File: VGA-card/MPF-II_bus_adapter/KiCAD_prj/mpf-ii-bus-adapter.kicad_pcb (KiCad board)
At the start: 2 copper layers, 98.5 x 35.6 mm, 36 parts, among them J1 Bus_Apple_II_Card_Side, J10 USER1_Sel, J11 INH_Sel, J12 RDY_Sel, J13 COLREF_Sel, J14 IOSTRB_Sel, J15 Q3_Sel, J16 Pin, J17 Pin, J18 Pin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

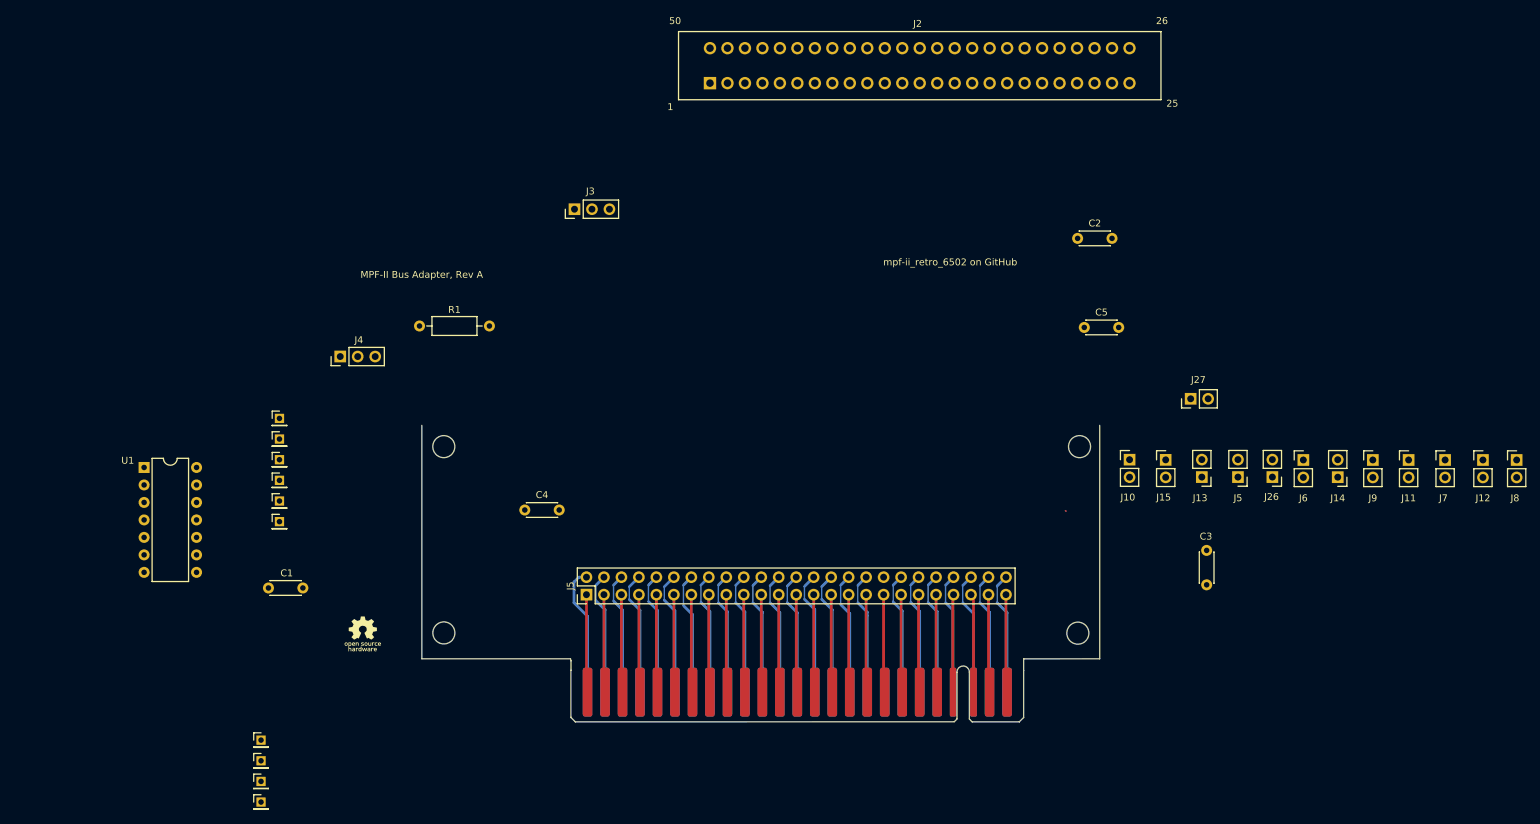
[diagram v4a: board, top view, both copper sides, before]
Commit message: Bus pin-header connector PCB
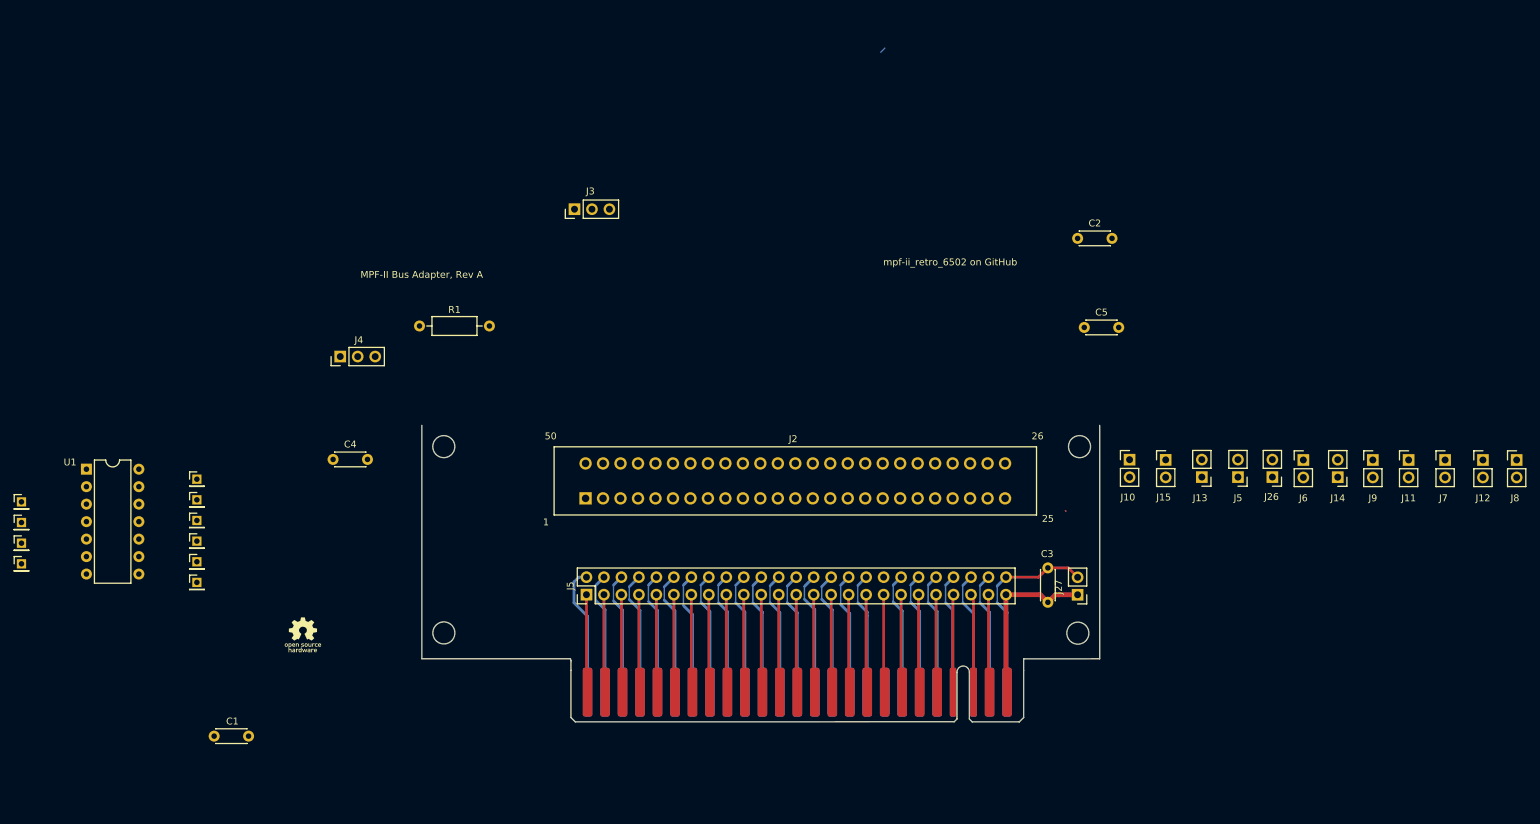
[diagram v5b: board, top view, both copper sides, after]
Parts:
- moved J2 63.0 mm to (118.7, 87.8)
- moved J16 49.1 mm to (36.7, 88.3)
- moved J17 49.1 mm to (36.7, 94.3)
- moved J24 49.1 mm to (36.7, 97.3)
- moved J25 49.1 mm to (36.7, 91.3)
- moved J27 32.9 mm to (190.2, 101.8), turned to 180 degrees
- moved C4 28.8 mm to (82.0, 82.2)
- moved C3 23.2 mm to (185.9, 102.9)
- moved C1 22.9 mm to (69.7, 122.4)
- moved J18 14.9 mm to (62.2, 97.0)
- moved J19 14.9 mm to (62.2, 91.0)
- moved J20 14.9 mm to (62.2, 85.0)
- moved J21 14.9 mm to (62.2, 88.0)
- moved J22 14.9 mm to (62.2, 94.0)
- moved J23 14.9 mm to (62.2, 100.0)
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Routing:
- net GND: track 18.1 -> 29.6 mm
- net +5V: track 14.2 -> 25.6 mm
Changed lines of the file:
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@@
 	(footprint "Capacitor_THT:C_Disc_D4.3mm_W1.9mm_P5.00mm"
 		(layer "F.Cu")
-		(at 208.94 100.4 90)
+		(at 185.87 102.94 90)
 		(descr "C, Disc series, Radial, pin pitch=5.00mm, , diameter*width=4.3*1.9mm^2, Capacitor, http://www.vishay.com/docs/45233/krseries.pdf")
 		(tags "C Disc series Radial pin pitch 5.00mm  diameter 4.3mm width 1.9mm Capacitor")
@@
 	(footprint "Capacitor_THT:C_Disc_D4.3mm_W1.9mm_P5.00mm"
 		(layer "F.Cu")
-		(at 109.86 89.53)
+		(at 82 82.18)
 		(descr "C, Disc series, Radial, pin pitch=5.00mm, , diameter*width=4.3*1.9mm^2, Capacitor, http://www.vishay.com/docs/45233/krseries.pdf")
 		(tags "C Disc series Radial pin pitch 5.00mm  diameter 4.3mm width 1.9mm Capacitor")
@@
 	(footprint "LOGO"
 		(layer "F.Cu")
-		(at 86.308751 107.644678)
+		(at 77.608751 107.784678)
 		(property "Reference" "G***"
 			(at 0 0 0)
@@
 	(footprint "Connector_PinHeader_2.00mm:PinHeader_1x01_P2.00mm_Vertical"
 		(layer "F.Cu")
-		(at 74.21 79.22)
+		(at 62.21 88.05)
 		(descr "Through hole straight pin header, 1x01, 2.00mm pitch, single row")
 		(tags "Through hole pin header THT 1x01 2.00mm single row")
@@
 	(footprint "Connector_PinHeader_2.00mm:PinHeader_1x01_P2.00mm_Vertical"
 		(layer "F.Cu")
-		(at 71.53 131.97)
+		(at 36.72 97.35)
 		(descr "Through hole straight pin header, 1x01, 2.00mm pitch, single row")
 		(tags "Through hole pin header THT 1x01 2.00mm single row")
@@
 	(footprint "Connector_PinHeader_2.00mm:PinHeader_1x01_P2.00mm_Vertical"
 		(layer "F.Cu")
-		(at 71.53 125.97)
+		(at 36.72 91.35)
 		(descr "Through hole straight pin header, 1x01, 2.00mm pitch, single row")
 		(tags "Through hole pin header THT 1x01 2.00mm single row")
@@
 	(footprint "PCM_MA_Connector_AppleII:EDAC_395-050-520-201_CounterClockwise"
 		(layer "F.Cu")
-		(at 136.77 27.5)
+		(at 118.69 87.84)
 		(descr "EDAC 395-050-520-201 Card Edge Connector - counter-clockwise pin numbering")
 		(tags "395-050-520-201 apple ii")
@@
 	(footprint "Capacitor_THT:C_Disc_D4.3mm_W1.9mm_P5.00mm"
 		(layer "F.Cu")
-		(at 77.61 100.86 180)
+		(at 69.72 122.39 180)
 		(descr "C, Disc series, Radial, pin pitch=5.00mm, , diameter*width=4.3*1.9mm^2, Capacitor, http://www.vishay.com/docs/45233/krseries.pdf")
 		(tags "C Disc series Radial pin pitch 5.00mm  diameter 4.3mm width 1.9mm Capacitor")
@@
 	(footprint "Connector_PinHeader_2.00mm:PinHeader_1x01_P2.00mm_Vertical"
 		(layer "F.Cu")
-		(at 74.21 88.22)
+		(at 62.21 97.05)
 		(descr "Through hole straight pin header, 1x01, 2.00mm pitch, single row")
 		(tags "Through hole pin header THT 1x01 2.00mm single row")
@@
 	(footprint "Connector_PinHeader_2.00mm:PinHeader_1x01_P2.00mm_Vertical"
 		(layer "F.Cu")
-		(at 74.21 91.22)
+		(at 62.21 100.05)
 		(descr "Through hole straight pin header, 1x01, 2.00mm pitch, single row")
 		(tags "Through hole pin header THT 1x01 2.00mm single row")
@@
 	(footprint "Connector_PinHeader_2.54mm:PinHeader_1x02_P2.54mm_Vertical"
 		(layer "F.Cu")
-		(at 206.62 73.37 90)
+		(at 190.19 101.845 180)
 		(descr "Through hole straight pin header, 1x02, 2.54mm pitch, single row")
 		(tags "Through hole pin header THT 1x02 2.54mm single row")
 		(property "Reference" "J27"
-			(at 2.76 1.115 0)
+			(at 2.76 1.115 90)
 			(layer "F.SilkS")
 			(effects
@@
 		)
 		(property "Value" "PWR"
-			(at 0 4.87 90)
+			(at 0 4.87 0)
 			(layer "F.Fab")
 			(hide yes)
@@
 		)
 		(property "Footprint" "Connector_PinHeader_2.54mm:PinHeader_1x02_P2.54mm_Vertical"
-			(at 0 0 90)
+			(at 0 0 180)
 			(unlocked yes)
 			(layer "F.Fab")
@@
 		)
 		(property "Datasheet" ""
-			(at 0 0 90)
+			(at 0 0 180)
 			(unlocked yes)
 			(layer "F.Fab")
@@
 		)
 		(property "Description" "Generic connector, single row, 01x02, script generated"
-			(at 0 0 90)
+			(at 0 0 180)
 			(unlocked yes)
 			(layer "F.Fab")
@@
 		(attr through_hole)
 		(fp_line
-			(start -1.33 -1.33)
-			(end 0 -1.33)
+			(start 1.33 1.27)
+			(end 1.33 3.87)
 			(stroke
 				(width 0.12)
@@
 		)
 		(fp_line
-			(start -1.33 0)
-			(end -1.33 -1.33)
+			(start -1.33 3.87)
+			(end 1.33 3.87)
 			(stroke
 				(width 0.12)
@@
 		)
 		(fp_line
-			(start 1.33 1.27)
-			(end 1.33 3.87)
+			(start -1.33 1.27)
+			(end 1.33 1.27)
 			(stroke
 				(width 0.12)
@@
 		(fp_line
 			(start -1.33 1.27)
-			(end 1.33 1.27)
+			(end -1.33 3.87)
 			(stroke
 				(width 0.12)
@@
 		)
 		(fp_line
-			(start -1.33 1.27)
-			(end -1.33 3.87)
+			(start -1.33 0)
+			(end -1.33 -1.33)
 			(stroke
 				(width 0.12)
@@
 		)
 		(fp_line
-			(start -1.33 3.87)
-			(end 1.33 3.87)
+			(start -1.33 -1.33)
+			(end 0 -1.33)
 			(stroke
 				(width 0.12)
@@
 		)
 		(fp_line
-			(start 1.8 -1.8)
-			(end -1.8 -1.8)
+			(start 1.8 4.35)
+			(end 1.8 -1.8)
 			(stroke
 				(width 0.05)
@@
 		)
 		(fp_line
-			(start -1.8 -1.8)
-			(end -1.8 4.35)
+			(start 1.8 -1.8)
+			(end -1.8 -1.8)
 			(stroke
 				(width 0.05)
@@
 		)
 		(fp_line
-			(start 1.8 4.35)
-			(end 1.8 -1.8)
+			(start -1.8 4.35)
+			(end 1.8 4.35)
 			(stroke
 				(width 0.05)
@@
 		)
 		(fp_line
-			(start -1.8 4.35)
-			(end 1.8 4.35)
+			(start -1.8 -1.8)
+			(end -1.8 4.35)
 			(stroke
 				(width 0.05)
@@
 		)
 		(fp_line
-			(start 1.27 -1.27)
-			(end 1.27 3.81)
+			(start 1.27 3.81)
+			(end -1.27 3.81)
 			(stroke
 				(width 0.1)
@@
 		)
 		(fp_line
-			(start -0.635 -1.27)
-			(end 1.27 -1.27)
+			(start 1.27 -1.27)
+			(end 1.27 3.81)
 			(stroke
 				(width 0.1)
@@
 		)
 		(fp_line
-			(start -1.27 -0.635)
-			(end -0.635 -1.27)
+			(start -0.635 -1.27)
+			(end 1.27 -1.27)
 			(stroke
 				(width 0.1)
@@
 		)
 		(fp_line
-			(start 1.27 3.81)
-			(end -1.27 3.81)
+			(start -1.27 3.81)
+			(end -1.27 -0.635)
 			(stroke
 				(width 0.1)
@@
 		)
 		(fp_line
-			(start -1.27 3.81)
-			(end -1.27 -0.635)
+			(start -1.27 -0.635)
+			(end -0.635 -1.27)
 			(stroke
 				(width 0.1)
@@
 		)
 		(fp_text user "${REFERENCE}"
-			(at 0 1.27 0)
+			(at 0 1.27 90)
 			(layer "F.Fab")
 			(effects
@@
 		)
 		(pad "1" thru_hole rect
-			(at 0 0 90)
+			(at 0 0 180)
 			(size 1.7 1.7)
 			(drill 1)
@@
 		)
 		(pad "2" thru_hole oval
-			(at 0 2.54 90)
+			(at 0 2.54 180)
 			(size 1.7 1.7)
 			(drill 1)
@@
 	(footprint "Connector_PinHeader_2.00mm:PinHeader_1x01_P2.00mm_Vertical"
 		(layer "F.Cu")
-		(at 71.53 122.97)
+		(at 36.72 88.35)
 		(descr "Through hole straight pin header, 1x01, 2.00mm pitch, single row")
 		(tags "Through hole pin header THT 1x01 2.00mm single row")
@@
 	(footprint "Connector_PinHeader_2.00mm:PinHeader_1x01_P2.00mm_Vertical"
 		(layer "F.Cu")
-		(at 71.53 128.97)
+		(at 36.72 94.35)
 		(descr "Through hole straight pin header, 1x01, 2.00mm pitch, single row")
 		(tags "Through hole pin header THT 1x01 2.00mm single row")
@@
 	(footprint "Connector_PinHeader_2.00mm:PinHeader_1x01_P2.00mm_Vertical"
 		(layer "F.Cu")
-		(at 74.21 76.22)
+		(at 62.21 85.05)
 		(descr "Through hole straight pin header, 1x01, 2.00mm pitch, single row")
 		(tags "Through hole pin header THT 1x01 2.00mm single row")
@@
 	(footprint "Package_DIP:DIP-14_W7.62mm"
 		(layer "F.Cu")
-		(at 54.54 83.35)
+		(at 46.16 83.6)
 		(descr "14-lead though-hole mounted DIP package, row spacing 7.62 mm (300 mils)")
 		(tags "THT DIP DIL PDIP 2.54mm 7.62mm 300mil")
@@
 	(footprint "Connector_PinHeader_2.00mm:PinHeader_1x01_P2.00mm_Vertical"
 		(layer "F.Cu")
-		(at 74.21 82.22)
+		(at 62.21 91.05)
 		(descr "Through hole straight pin header, 1x01, 2.00mm pitch, single row")
 		(tags "Through hole pin header THT 1x01 2.00mm single row")
@@
 	(footprint "Connector_PinHeader_2.00mm:PinHeader_1x01_P2.00mm_Vertical"
 		(layer "F.Cu")
-		(at 74.21 85.22)
+		(at 62.21 94.05)
 		(descr "Through hole straight pin header, 1x01, 2.00mm pitch, single row")
 		(tags "Through hole pin header THT 1x01 2.00mm single row")
@@
 	)
 	(segment
+		(start 186.96 101.85)
+		(end 187.55 101.85)
+		(width 0.7)
+		(layer "F.Cu")
+		(net 1)
+	)
+	(segment
 		(start 179.78 101.83)
 		(end 179.78 115.84)
-		(width 0.4)
+		(width 0.7)
 		(layer "F.Cu")
 		(net 1)
@@
 	)
 	(segment
+		(start 179.78 101.83)
+		(end 184.76 101.83)
+		(width 0.7)
+		(layer "F.Cu")
+		(net 1)
+	)
+	(segment
+		(start 187.555 101.845)
+		(end 190.19 101.845)
+		(width 0.7)
+		(layer "F.Cu")
+		(net 1)
+	)
+	(segment
+		(start 187.55 101.85)
+		(end 187.555 101.845)
+		(width 0.7)
+		(layer "F.Cu")
+		(net 1)
+	)
+	(segment
+		(start 190.155 101.83)
+		(end 190.19 101.795)
+		(width 0.4)
+		(layer "F.Cu")
+		(net 1)
+	)
+	(segment
+		(start 185.87 102.94)
+		(end 186.96 101.85)
+		(width 0.7)
+		(layer "F.Cu")
+		(net 1)
+	)
+	(segment
+		(start 184.76 101.83)
+		(end 185.87 102.94)
+		(width 0.7)
+		(layer "F.Cu")
+		(net 1)
+	)
+	(segment
+		(start 179.78 99.29)
+		(end 184.52 99.29)
+		(width 0.4)
+		(layer "F.Cu")
+		(net 2)
+	)
+	(segment
+		(start 184.52 99.29)
+		(end 185.87 97.94)
+		(width 0.4)
+		(layer "F.Cu")
+		(net 2)
+	)
+	(segment
+		(start 190.155 99.29)
+		(end 190.19 99.255)
+		(width 0.4)
+		(layer "F.Cu")
+		(net 2)
+	)
+	(segment
 		(start 188.42 89.63)
 		(end 188.5 89.71)
@@
 	)
 	(segment
+		(start 185.87 97.94)
+		(end 188.825 97.94)
+		(width 0.4)
+		(layer "F.Cu")
+		(net 2)
+	)
+	(segment
+		(start 188.825 97.94)
+		(end 190.19 99.305)
+		(width 0.4)
+		(layer "F.Cu")
+		(net 2)
+	)
+	(segment
 		(start 178.5 100.57)
 		(end 178.5 103)
@@
 	)
 	(segment
-		(start 73.88 81.89)
-		(end 74.21 82.22)
+		(start 61.88 90.72)
+		(end 62.21 91.05)
 		(width 0.2)
 		(layer "F.Cu")
@@
 	)
 	(segment
-		(start 73.62 76.81)
-		(end 74.21 76.22)
+		(start 61.62 85.64)
+		(end 62.21 85.05)
 		(width 0.2)
 		(layer "F.Cu")
@@
 	)
 	(segment
-		(start 74.08 79.35)
-		(end 74.21 79.22)
+		(start 62.08 88.18)
+		(end 62.21 88.05)
 		(width 0.2)
 		(layer "F.Cu")

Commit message: PCB
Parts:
- removed J18, J19, J20, J21, J22, J23, J24, J25: Pin, Connector_PinHeader_2.00mm:PinHeader_1x01_P2.00mm_Vertical
- J16: value Pin -> Conn_01x04_Pin; footprint Connector_PinHeader_2.00mm:PinHeader_1x01_P2.00mm_Vertical -> Connector_PinHeader_2.54mm:PinHeader_1x04_P2.54mm_Vertical
- J17: value Pin -> Conn_01x06_Pin; footprint Connector_PinHeader_2.00mm:PinHeader_1x01_P2.00mm_Vertical -> Connector_PinHeader_2.54mm:PinHeader_1x06_P2.54mm_Vertical
- moved G*** 106.5 mm to (184.1, 107.2)
- moved J17 75.1 mm to (111.8, 93.8)
- moved J16 60.3 mm to (97.0, 91.4)
- moved U1 54.0 mm to (100.1, 86.3)
- moved J10 48.1 mm to (150.1, 75.6), turned to 90 degrees
- moved J15 45.5 mm to (157.9, 75.7), turned to 90 degrees
- moved R1 43.4 mm to (136.0, 75.7), turned to 180 degrees
- moved C1 42.4 mm to (108.3, 104.9)
- moved J3 37.8 mm to (140.3, 75.7)
- moved J13 34.5 mm to (174.9, 75.8), turned to -90 degrees
- moved J4 34.5 mm to (116.5, 75.8)
- moved C2 33.6 mm to (168.8, 76.0), turned to 180 degrees
- moved C5 28.8 mm to (190.3, 91.8), turned to 90 degrees
- moved C4 22.9 mm to (104.5, 77.5), turned to -90 degrees
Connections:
- U1 pad 10: Net-(J22-Pin_1) -> Net-(J17-Pin_4)
- U1 pad 11: Net-(J19-Pin_1) -> Net-(J17-Pin_3)
- U1 pad 12: Net-(J21-Pin_1) -> Net-(J17-Pin_2)
- U1 pad 13: Net-(J20-Pin_1) -> Net-(J17-Pin_1)
- U1 pad 4: Net-(J25-Pin_1) -> Net-(J16-Pin_2)
- U1 pad 5: Net-(J17-Pin_1) -> Net-(J16-Pin_3)
- U1 pad 6: Net-(J24-Pin_1) -> Net-(J16-Pin_4)
- U1 pad 8: Net-(J23-Pin_1) -> Net-(J17-Pin_6)
- U1 pad 9: Net-(J18-Pin_1) -> Net-(J17-Pin_5)
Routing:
- net +5V: track 25.6 -> 179.9 mm
- net GND: track 29.6 -> 93.7 mm
- net Net-(J4-Pin_1): track 0.00 -> 24.3 mm
- net +12V: track 18.9 -> 37.1 mm
- net /IOSEL: track 15.0 -> 30.2 mm
- net Net-(J17-Pin_2): track 0.00 -> 8.02 mm
- net Net-(J17-Pin_6): track 0.00 -> 7.40 mm
- net Net-(J17-Pin_5): track 0.00 -> 7.33 mm
- net Net-(J17-Pin_3): track 0.00 -> 7.30 mm
- net Net-(J17-Pin_4): track 0.00 -> 7.16 mm
- net Net-(J17-Pin_1): track 0.00 -> 6.70 mm
- net Net-(J16-Pin_3): track 0.00 -> 3.13 mm
- net Net-(J16-Pin_1): track 0.00 -> 3.13 mm
- net Net-(J16-Pin_4): track 0.00 -> 3.13 mm
- net Net-(J16-Pin_2): track 0.00 -> 3.13 mm
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
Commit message: PCB updated
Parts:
- removed the J5 at (213.5, 84.7)
- moved J26 77.7 mm to (141.5, 95.5)
- moved J6 77.0 mm to (146.8, 93.0)
- moved J9 76.8 mm to (157.0, 93.0)
- moved J14 76.8 mm to (152.0, 95.5)
- moved J11 76.5 mm to (162.5, 93.0)
- moved J7 76.3 mm to (168.0, 93.0)
- moved J12 76.1 mm to (173.8, 93.0)
- moved J8 75.3 mm to (179.5, 93.0)
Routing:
- net /D1: track 17.7 -> 35.4 mm
- net /D0: track 17.7 -> 35.3 mm
- net /A1: track 14.2 -> 29.4 mm
- net /A0: track 17.6 -> 32.7 mm
- net +5V: track 179.9 -> 176.8 mm
- net Net-(J4-Pin_1): track 24.3 -> 26.9 mm
- net /EXTE: track 17.8 -> 17.0 mm

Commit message: PCB updated
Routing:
- net GND: track 94.0 -> 175.5 mm, vias 0 -> 1
- net /PHI1: track 17.9 -> 72.4 mm, vias 0 -> 1
- net /A_PHI0: track 0.00 -> 34.6 mm, vias 0 -> 1
- net /A8: track 14.2 -> 32.2 mm
- net /D3: track 17.7 -> 35.4 mm
- net /D4: track 17.9 -> 35.6 mm
- net /D6: track 17.7 -> 35.3 mm
- net /D5: track 17.7 -> 35.3 mm
- net /D2: track 17.9 -> 35.5 mm
- net /D7: track 17.7 -> 35.3 mm
- net /A2: track 14.2 -> 29.4 mm
- net /A5: track 14.2 -> 29.3 mm
- net /A7: track 14.2 -> 29.2 mm
- net /A3: track 14.2 -> 29.2 mm
- net /A6: track 14.2 -> 29.2 mm
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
